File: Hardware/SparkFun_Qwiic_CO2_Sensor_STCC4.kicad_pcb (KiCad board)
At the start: 2 copper layers, 25.4 x 25.4 mm, 45 parts, among them J1 Qwiic_RA, J2 Qwiic_RA, J3 Conn_01x06, U2 STCC4, U3 SHT40

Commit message: Finalized the Silkscreen
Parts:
- removed the G*** at (136.0, 96.8)
- added kibuzzard-6A0B3951: G***, kibuzzard-6A0B3951, B.Cu at (139.7, 88.8)
- added kibuzzard-6A0B3970: G***, kibuzzard-6A0B3970, B.Cu at (139.7, 87.7)
- moved Ref** 9.14 mm to (136.0, 97.2)
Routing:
- net GND: vias 20 -> 24

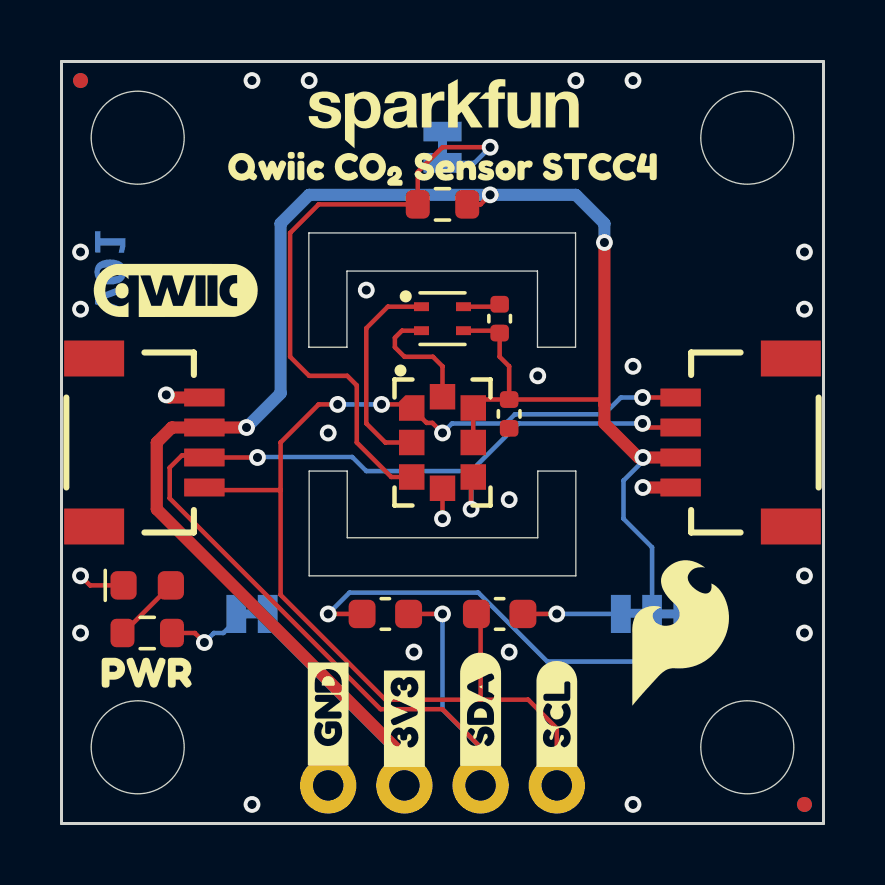
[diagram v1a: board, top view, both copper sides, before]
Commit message: Added changes from Design Review
- Nudged vias
- Replaced "pullup" capacitors
- Adjusted measures alignment
- Adjusted solder paste expansion
- Swapped Flame and OSHW Logos
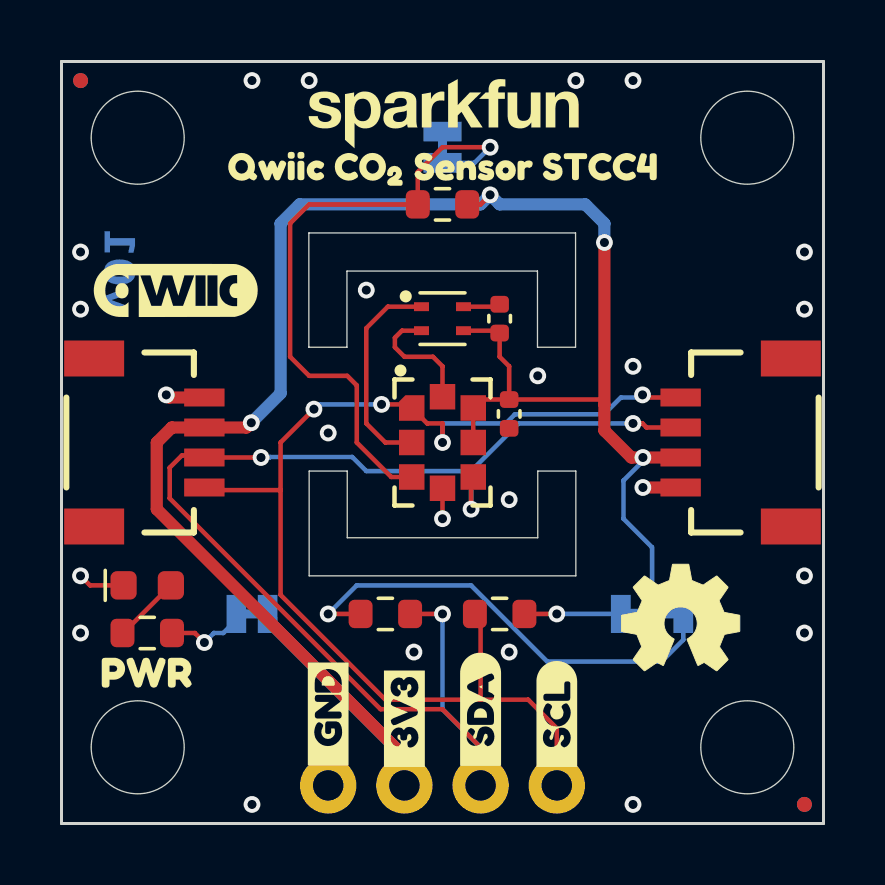
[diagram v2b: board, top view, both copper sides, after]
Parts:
- G***: moved to B.Cu
- R4, R5: value 0.1uF -> 2.2k; footprint SparkFun-Capacitor:C_0603_1608Metric -> SparkFun-Resistor:R_0603_1608Metric
- Ref**: moved to F.Cu
- moved G*** 11.0 mm to (136.0, 96.8), turned to 180 degrees
- moved Ref** 10.6 mm to (143.9, 104.1), turned to 0 degrees
- turned R4 to 180 degrees
- turned R5 to 0 degrees
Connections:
- R4 pad 1: SCL -> Net-(JP2-C)
- R4 pad 2: Net-(JP2-C) -> SCL
- R5 pad 1: SDA -> Net-(JP2-A)
- R5 pad 2: Net-(JP2-A) -> SDA
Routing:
- net SCL: track 38.6 -> 39.7 mm

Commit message: Updates Edge Cut polygon to an outline and adds "Route Out" to ensure proper manufacturing
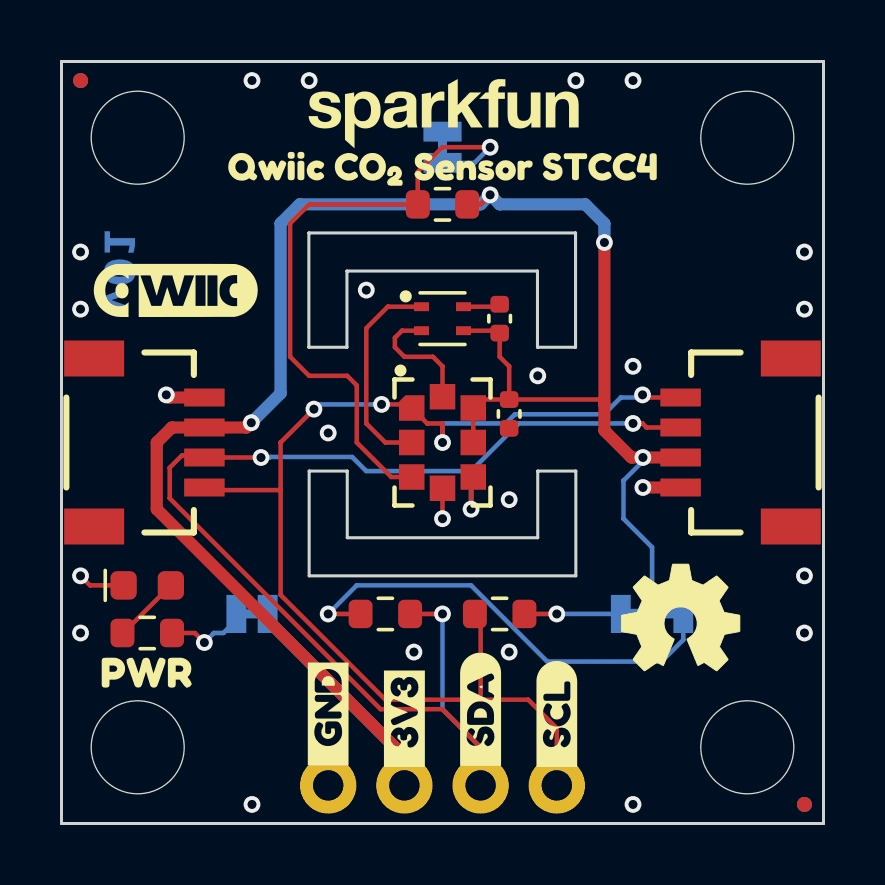
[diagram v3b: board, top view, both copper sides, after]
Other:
- board text added: "Route Out"
